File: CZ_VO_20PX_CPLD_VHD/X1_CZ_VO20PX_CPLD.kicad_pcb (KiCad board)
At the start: 2 copper layers, 137 x 140 mm, 112 parts, among them IC1 EMP7064_PLCC84, IC10 4538, IC100 ATmega328P-PU, IC101 ATmega328P-PU, IC102 4069, IC11 4013, IC120 LM1881, IC2 8251, IC3 74LS245, IC4 74LS393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

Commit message: Add files via upload
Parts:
- IC11: footprint Package_DIP:DIP-14_W10.16mm_LongPads -> Package_DIP:DIP-14_W7.62mm_Socket_LongPads
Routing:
- net 5V: track 647.7 -> 643.3 mm

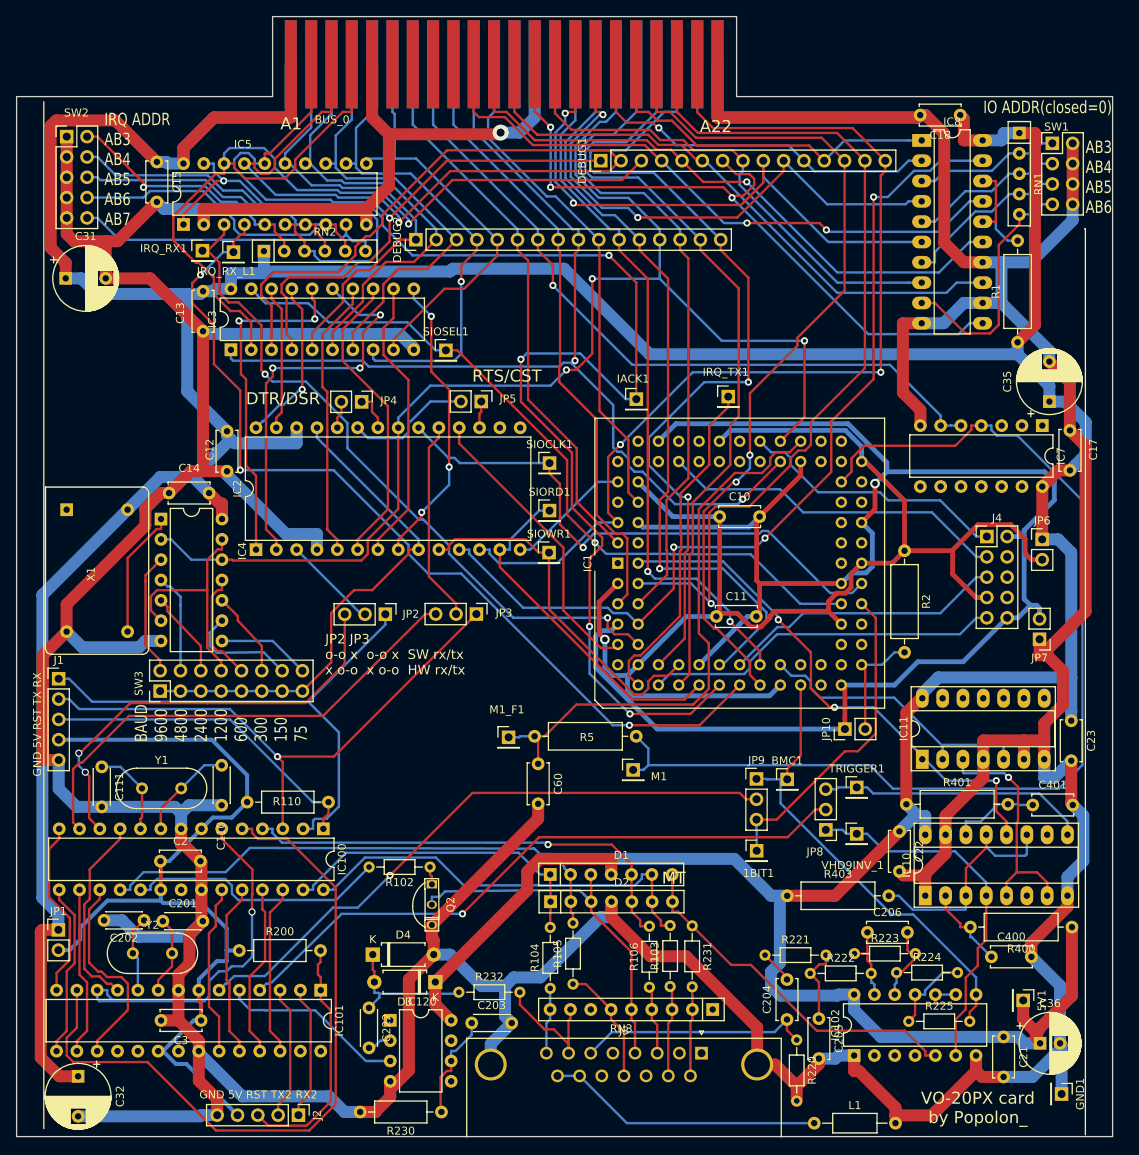
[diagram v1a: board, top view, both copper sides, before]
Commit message: corrected rx/tx mapping
corrected rx/tx mapping betwene atmega328p and 8251
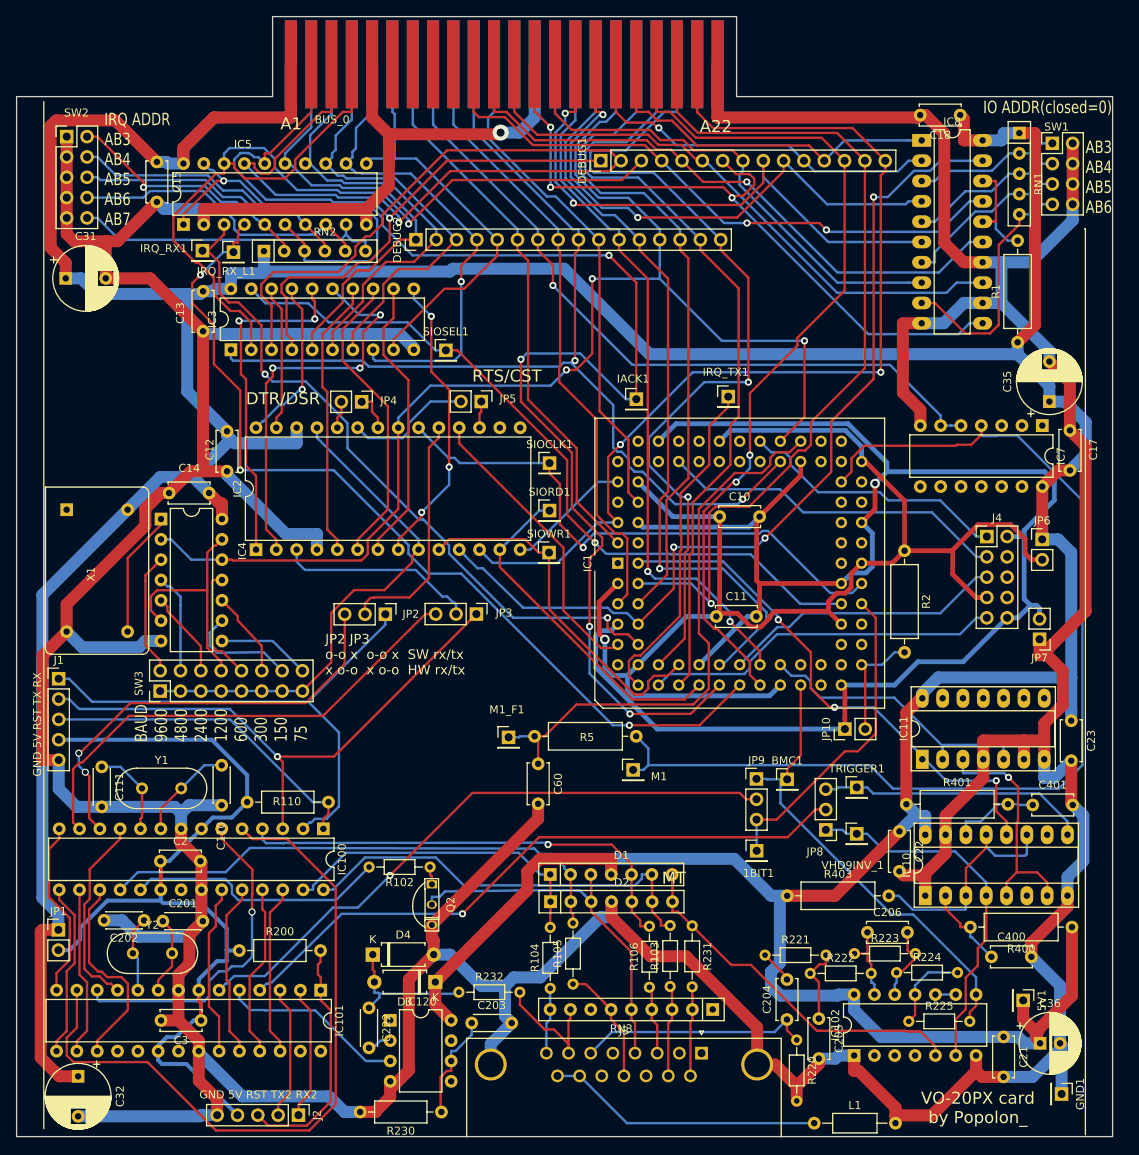
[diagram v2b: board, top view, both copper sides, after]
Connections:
- JP2 pad 2: Net-(IC2-Pad3) -> Net-(IC2-Pad19)
- JP3 pad 2: Net-(IC2-Pad19) -> Net-(IC2-Pad3)
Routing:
- net Net-(IC2-Pad3): track 11.9 -> 24.8 mm
- net Net-(IC2-Pad19): track 25.2 -> 30.4 mm
- net VHD_DATA_ACK: track 48.1 -> 45.2 mm
- net ARDUINO_POWER: track 108.5 -> 110.1 mm
- net Net-(IC5-Pad5): track 32.6 -> 31.5 mm
- net Net-(IC5-Pad8): track 39.0 -> 37.9 mm
- net Net-(IC5-Pad7): track 35.1 -> 34.2 mm
- net M1: track 134.7 -> 135.4 mm
- net ~SIORD: track 43.6 -> 42.9 mm
- net RX: track 68.2 -> 67.6 mm
- net ~IACK: track 164.9 -> 164.4 mm
- net VHD3BIT: track 57.6 -> 58.1 mm

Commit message: Add files via upload
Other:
- board text added: "100K"
- board text added: "10K"
- board text added: "180R"
- board text added: "1M"
- board text added: "1nF"
- board text added: "2.2nF"
- board text added: "220R"
- board text added: "22K"
- board text added: "22pF"
- board text added: "330pF"
- board text added: "390pF"
- board text added: "4013"
- board text added: "4069"
- board text added: "4538"
- board text added: "4K7"
- board text added: "5K6"
- board text added: "5V"
- board text added: "680K"
- board text added: "680pF"
- board text added: "8251"
- board text added: "BC635"
- board text added: "GND"
- board text added: "IO ADDR(closed=0) A4 A5 A6 A7"
- board text added: "IRQ ADDR(closed = 0 ) A3 A4 A5 A6 A7"
- board text added: "LS02"
- board text added: "LS245"
- board text added: "LS393"
- board text added: "LS541"
- board text added: "LS688"
- board text added: "PLCC 5V"
- board text added: "PLCC GND"
- board text added: "TCK"
- board text added: "TDI"
- board text added: "TDO"
- board text added: "TMS"
- board text added: "VCC"
- board text removed: "IO ADDR(closed=0) AB3 AB4 AB5 AB6"
- board text removed: "IRQ ADDR AB3 AB4 AB5 AB6 AB7"

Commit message: Add files via upload
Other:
- board text added: "ATF1504AS"
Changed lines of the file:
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@@
   (general
     (thickness 1.6)
-    (drawings 72)
+    (drawings 73)
     (tracks 2256)
     (zones 0)
@@
     )
   )
+  (gr_text ATF1504AS (at 218.5416 161.0868) (layer F.SilkS)
+    (effects (font (size 1.5 1.5) (thickness 0.3)))
+  )
   (gr_text 10K (at 256.4003 126.5174 90) (layer F.SilkS)

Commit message: Add files via upload
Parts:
- removed C17, C23: 100nF, Capacitor_THT:C_Disc_D5.0mm_W2.5mm_P5.00mm
- removed C203, C222: 100nF, Capacitor_THT:C_Disc_D4.3mm_W1.9mm_P5.00mm
- removed IC11: 4013, Package_DIP:DIP-14_W7.62mm_Socket_LongPads
- removed IC120: LM1881, Package_DIP:DIP-8_W7.62mm
- removed IC7: 74LS02, Package_DIP:DIP-14_W7.62mm
- removed JP8: Jumper_3_Open, Connector_PinHeader_2.54mm:PinHeader_1x03_P2.54mm_Vertical
- removed R230: 680K, Resistor_THT:R_Axial_DIN0207_L6.3mm_D2.5mm_P10.16mm_Horizontal
- removed SW3: CONN_02x08, Connector_PinHeader_2.54mm:PinHeader_2x08_P2.54mm_Vertical
- Q2: value NPN (D637) or BC635 -> NPN (BC546)
- R110: footprint Resistor_THT:R_Axial_DIN0207_L6.3mm_D2.5mm_P10.16mm_Horizontal -> Resistor_THT:R_Axial_DIN0207_L6.3mm_D2.5mm_P7.62mm_Horizontal
- R2, R5: footprint Resistor_THT:R_Axial_DIN0309_L9.0mm_D3.2mm_P12.70mm_Horizontal -> Resistor_THT:R_Axial_DIN0207_L6.3mm_D2.5mm_P7.62mm_Horizontal
- R400, R401, R403: footprint Resistor_THT:R_Axial_DIN0309_L9.0mm_D3.2mm_P12.70mm_Horizontal -> Resistor_THT:R_Axial_DIN0204_L3.6mm_D1.6mm_P7.62mm_Horizontal
- moved C60 64.0 mm to (234.6, 137.6), turned to 90 degrees
- moved M1_F1 59.6 mm to (230.9, 140.3)
- moved M1 56.6 mm to (241.4, 143.8)
- moved R5 56.1 mm to (241.9, 140.3)
- moved IC4 17.2 mm to (153.7, 171.2), turned to 180 degrees
- moved C401 5.41 mm to (249.6, 191.5)
- moved C400 3.75 mm to (249.9, 206.8), turned to 180 degrees
- moved C14 3.53 mm to (148.6, 152.9), turned to 0 degrees
- moved Q2 2.83 mm to (178.5, 203.9), turned to 180 degrees
- moved J1 1.40 mm to (134.6, 176.4)
- moved C12 1.34 mm to (154.6, 143.5)
- moved R401 0.64 mm to (239.2, 192.1)
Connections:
- D3 pad 2: Net-(C222-Pad1) -> Net-(D3-Pad2)
- D4 pad 1: Net-(C222-Pad1) -> Net-(D3-Pad2)
- IC1 pad 52: M1 -> (no net)
- IC1 pad 54: (no net) -> M1
- IC1 pad 56: (no net) -> M1_FILTERED
- IC1 pad 58: M1_FILTERED -> ~M1
- IC10 pad 4: VHD9_INV -> ~VHD9_PACKET_SYNC
- IC10 pad 5: Net-(IC10-Pad5) -> DCLK1
- IC10 pad 7: Net-(IC10-Pad5) -> DCLK1
- IC101 pad 18: (no net) -> Net-(IC101-Pad18)
- IC101 pad 4: Net-(IC101-Pad4) -> VHD_1BIT_TRIGGER
- IC101 pad 5: V_SYNCH -> ~VHD9_PACKET_SYNC
- IC101 pad 6: Net-(IC101-Pad6) -> ~COMPOSITE_SYNCH
- IC102 pad 3: (no net) -> Net-(D3-Pad2)
- IC102 pad 4: (no net) -> ~COMPOSITE_SYNCH
- IC102 pad 6: VHD9_INV -> ~VHD9_PACKET_SYNC
- IC4 pad 10: Net-(IC4-Pad10) -> (no net)
- IC4 pad 11: Net-(IC4-Pad11) -> (no net)
- IC4 pad 12: RESET -> (no net)
- IC4 pad 13: Net-(IC4-Pad13) -> (no net)
- IC4 pad 3: Net-(IC4-Pad3) -> TxRxCLK
- IC4 pad 4: Net-(IC4-Pad4) -> (no net)
- IC4 pad 5: Net-(IC4-Pad5) -> (no net)
- IC4 pad 6: Net-(IC4-Pad13) -> (no net)
- IC4 pad 8: Net-(IC4-Pad8) -> (no net)
- IC4 pad 9: Net-(IC4-Pad9) -> (no net)
- JP9 pad 2: Net-(IC101-Pad6) -> Net-(IC101-Pad18)
- Q2 pad 1: Net-(Q2-Pad1) -> VHD4
- Q2 pad 2: VHD4 -> Net-(Q2-Pad2)
- R102 pad 1: Net-(Q2-Pad1) -> Net-(Q2-Pad2)
- R232 pad 1: Net-(C222-Pad1) -> Net-(D3-Pad2)
- VHD9INV_1 pad 1: VHD9_INV -> ~VHD9_PACKET_SYNC
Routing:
- net ~VHD9_PACKET_SYNC: track 0.00 -> 141.9 mm, vias 0 -> 1
- net M1: track 135.4 -> 14.9 mm
- net Net-(IC101-Pad18): track 0.00 -> 108.7 mm
- net ~COMPOSITE_SYNCH: track 0.00 -> 97.2 mm
- net VHD_1BIT_TRIGGER: track 33.7 -> 116.0 mm, vias 0 -> 1
- net Net-(IC101-Pad4): track 80.1 -> 0.00 mm, vias 1 -> 0
- net Net-(D3-Pad2): track 0.00 -> 78.6 mm
- net Net-(IC101-Pad6): track 77.7 -> 0.00 mm, vias 1 -> 0
- net M1_FILTERED: track 70.7 -> 13.2 mm
- net GND: track 850.5 -> 794.5 mm, vias 1 -> 2
- net VHD9_INV: track 46.0 -> 0.00 mm
- net 5V: track 643.3 -> 597.7 mm
- net DB0: track 120.4 -> 162.7 mm
- net Net-(IC2-Pad1): track 43.0 -> 82.1 mm, vias 2 -> 0
- net DB1: track 137.6 -> 101.8 mm, vias 1 -> 2
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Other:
- board text added: "AB10"
- board text added: "AB11"
- board text added: "AB9 AB8 AB7 AB6 AB5 AB4 AB3 AB2 AB1 AB0"
- board text added: "DB2 DB1 DB0"
- board text added: "DB3 DB4 DB5 DB6 DB7 CLK M1 ~WE~ RD"
- board text added: "~IORQ~ ~IEI~ ~IEO~ RST ~EXIO~ ~EXINT~ ~EXWAIT"
- board text removed: "4013"
- board text removed: "680K"
- board text removed: "BAUD 9600 4800 2400 1200 600 300 150 75"
- board text removed: "LS02"
